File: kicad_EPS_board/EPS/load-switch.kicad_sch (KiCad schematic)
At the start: 18 parts, among them Q1 IPA045N10N3G, T1 BC846B, U1 INA186

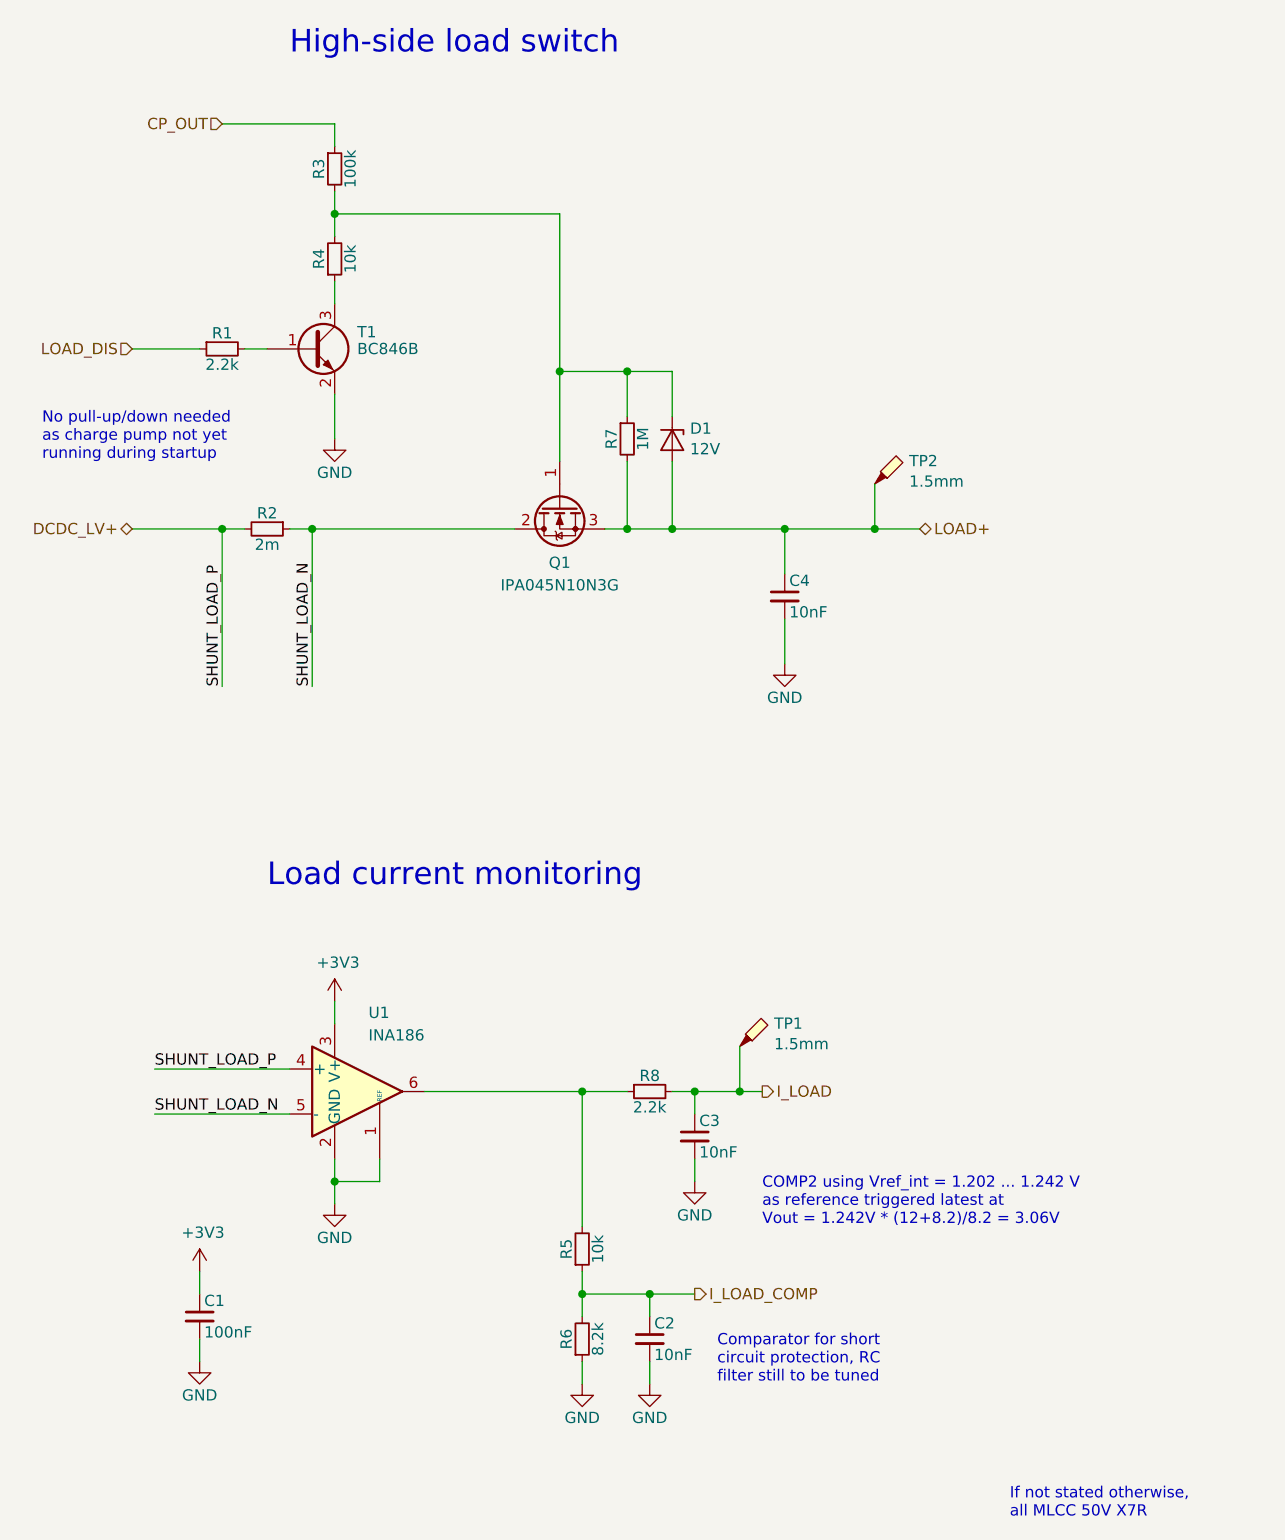
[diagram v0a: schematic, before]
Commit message: kicad EPS board V2 revision and already generated html doc files
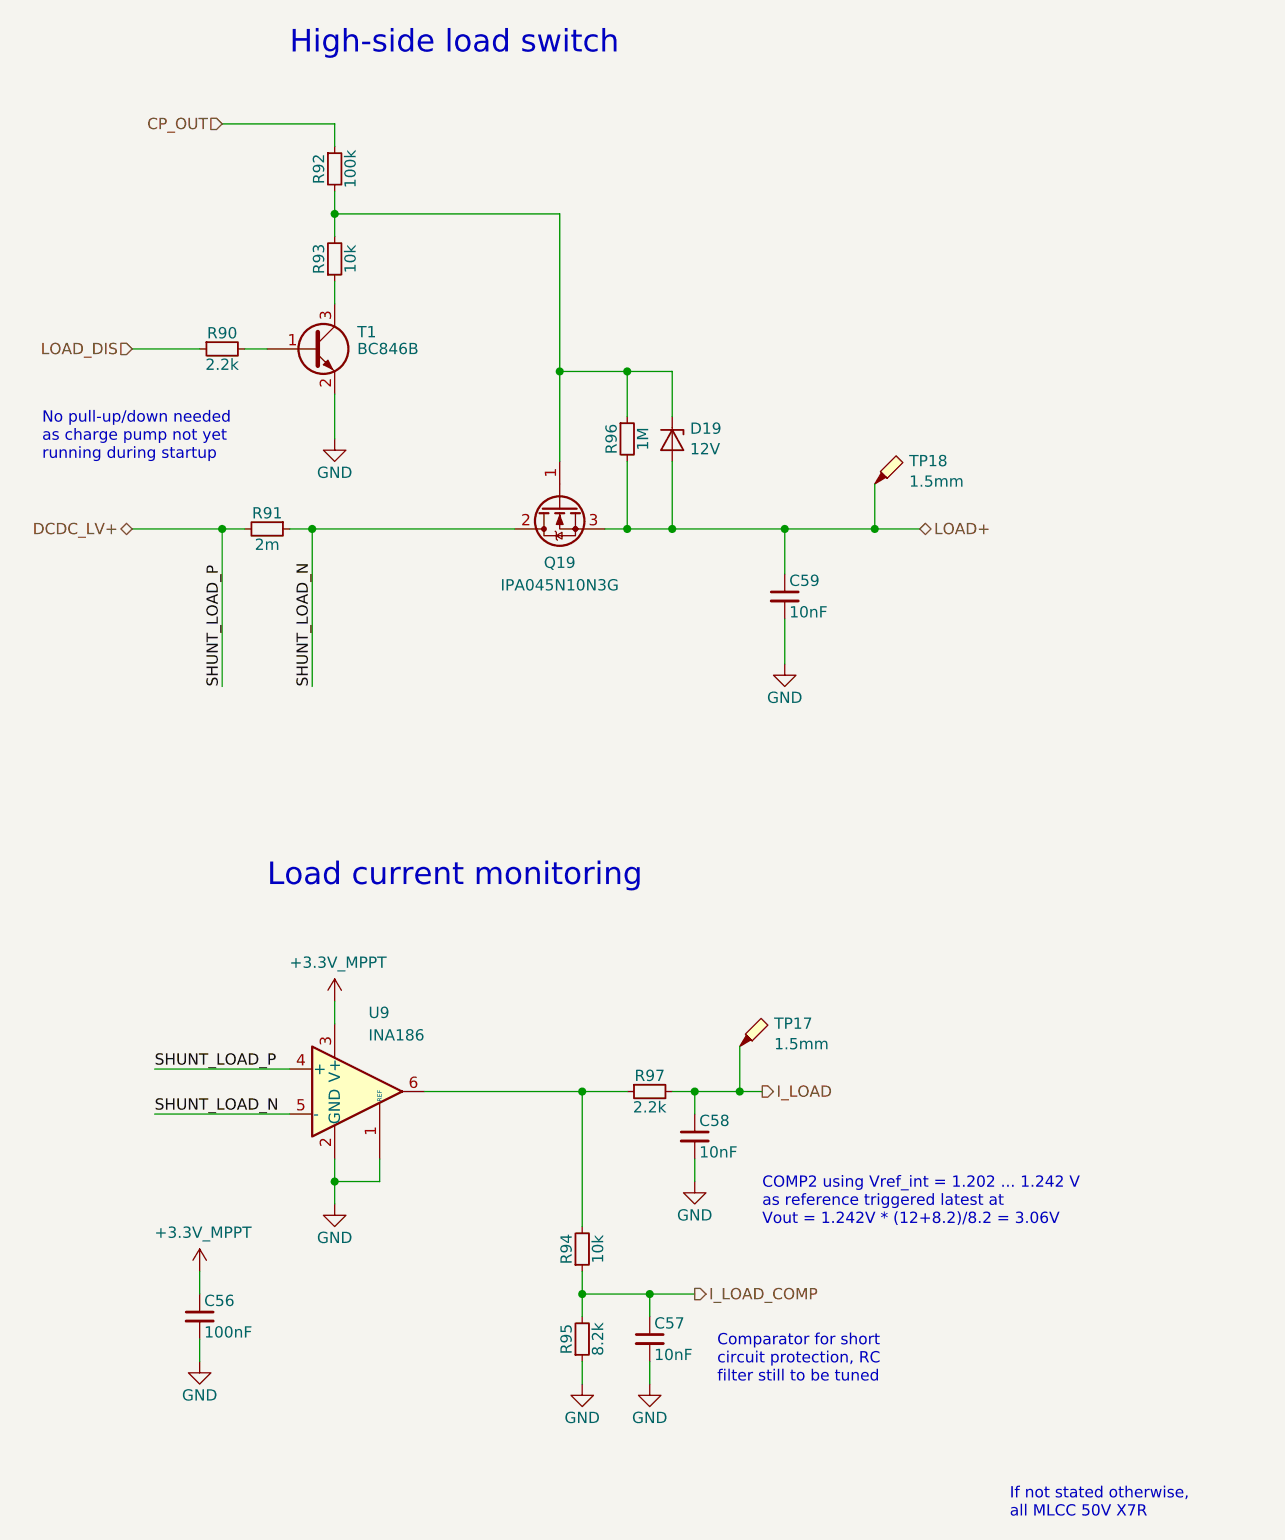
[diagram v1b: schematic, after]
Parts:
- renumbered C1 to C56, C2 to C57, C3 to C58, C4 to C59, D1 to D19, Q1 to Q19, R1 to R90, R2 to R91, R3 to R92, R4 to R93, R5 to R94, R6 to R95, R7 to R96, R8 to R97, TP1 to TP17, TP2 to TP18, U1 to U9
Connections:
- net +3V3 renamed +3.3V_MPPT
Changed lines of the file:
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@@
 (kicad_sch
-	(version 20231120)
+	(version 20250114)
 	(generator "eeschema")
-	(generator_version "8.0")
+	(generator_version "9.0")
 	(paper "A4")
+	(text "Load current monitoring"
+		(exclude_from_sim no)
+		(at 57.15 114.3 0)
+		(effects
+			(font
+				(size 2.54 2.54)
+			)
+			(justify left bottom)
+		)
+	)
+	(text "No pull-up/down needed\nas charge pump not yet \nrunning during startup"
+		(exclude_from_sim no)
+		(at 31.75 66.04 0)
+		(effects
+			(font
+				(size 1.27 1.27)
+			)
+			(justify left bottom)
+		)
+	)
+	(text "If not stated otherwise,\nall MLCC 50V X7R"
+		(exclude_from_sim no)
+		(at 140.97 185.42 0)
+		(effects
+			(font
+				(size 1.27 1.27)
+			)
+			(justify left bottom)
+		)
+	)
+	(text "Comparator for short \ncircuit protection, RC\nfilter still to be tuned"
+		(exclude_from_sim no)
+		(at 107.95 170.18 0)
+		(effects
+			(font
+				(size 1.27 1.27)
+			)
+			(justify left bottom)
+		)
+	)
+	(text "High-side load switch"
+		(exclude_from_sim no)
+		(at 59.69 20.32 0)
+		(effects
+			(font
+				(size 2.54 2.54)
+			)
+			(justify left bottom)
+		)
+	)
+	(text "COMP2 using Vref_int = 1.202 ... 1.242 V\nas reference triggered latest at\nVout = 1.242V * (12+8.2)/8.2 = 3.06V"
+		(exclude_from_sim no)
+		(at 113.03 152.4 0)
+		(effects
+			(font
+				(size 1.27 1.27)
+			)
+			(justify left bottom)
+		)
+	)
 	(junction
 		(at 62.23 73.66)
@@
 			(width 0)
 			(type default)
-		)
-	)
-	(text "Load current monitoring"
-		(exclude_from_sim no)
-		(at 57.15 114.3 0)
-		(effects
-			(font
-				(size 2.54 2.54)
-			)
-			(justify left bottom)
-		)
-	)
-	(text "No pull-up/down needed\nas charge pump not yet \nrunning during startup"
-		(exclude_from_sim no)
-		(at 31.75 66.04 0)
-		(effects
-			(font
-				(size 1.27 1.27)
-			)
-			(justify left bottom)
-		)
-	)
-	(text "If not stated otherwise,\nall MLCC 50V X7R"
-		(exclude_from_sim no)
-		(at 140.97 185.42 0)
-		(effects
-			(font
-				(size 1.27 1.27)
-			)
-			(justify left bottom)
-		)
-	)
-	(text "Comparator for short \ncircuit protection, RC\nfilter still to be tuned"
-		(exclude_from_sim no)
-		(at 107.95 170.18 0)
-		(effects
-			(font
-				(size 1.27 1.27)
-			)
-			(justify left bottom)
-		)
-	)
-	(text "High-side load switch"
-		(exclude_from_sim no)
-		(at 59.69 20.32 0)
-		(effects
-			(font
-				(size 2.54 2.54)
-			)
-			(justify left bottom)
-		)
-	)
-	(text "COMP2 using Vref_int = 1.202 ... 1.242 V\nas reference triggered latest at\nVout = 1.242V * (12+8.2)/8.2 = 3.06V"
-		(exclude_from_sim no)
-		(at 113.03 152.4 0)
-		(effects
-			(font
-				(size 1.27 1.27)
-			)
-			(justify left bottom)
 		)
 	)
@@
 		(on_board yes)
 		(dnp no)
-		(property "Reference" "C2"
+		(property "Reference" "C57"
 			(at 100.838 163.322 0)
 			(effects
@@
 		(on_board yes)
 		(dnp no)
-		(property "Reference" "TP1"
+		(property "Reference" "TP17"
 			(at 114.3762 129.4892 0)
 			(effects
@@
 		(on_board yes)
 		(dnp no)
-		(property "Reference" "TP2"
+		(property "Reference" "TP18"
 			(at 129.6162 65.9892 0)
 			(effects
@@
 		(on_board yes)
 		(dnp no)
-		(property "Reference" "#PWR03"
+		(property "Reference" "#PWR095"
 			(at 64.77 69.85 0)
 			(effects
@@
 		(on_board yes)
 		(dnp no)
-		(property "Reference" "R3"
+		(property "Reference" "R92"
 			(at 62.992 33.02 90)
 			(effects
@@
 		(on_board yes)
 		(dnp no)
-		(property "Reference" "R2"
+		(property "Reference" "R91"
 			(at 57.15 71.882 90)
 			(effects
@@
 		(on_board yes)
 		(dnp no)
-		(property "Reference" "C4"
+		(property "Reference" "C59"
 			(at 116.078 79.502 0)
 			(effects
@@
 		(on_board yes)
 		(dnp no)
-		(property "Reference" "D1"
+		(property "Reference" "D19"
 			(at 104.8766 62.3316 90)
 			(effects
@@
 		(on_board yes)
 		(dnp no)
-		(property "Reference" "R4"
+		(property "Reference" "R93"
 			(at 62.992 43.18 90)
 			(effects
@@
 		(on_board yes)
 		(dnp no)
-		(property "Reference" "#PWR02"
+		(property "Reference" "#PWR094"
 			(at 49.53 173.99 0)
 			(effects
@@
 		(on_board yes)
 		(dnp no)
-		(property "Reference" "R6"
+		(property "Reference" "R95"
 			(at 90.932 165.1 90)
 			(effects
@@
 		(on_board yes)
 		(dnp no)
-		(property "Reference" "#PWR01"
+		(property "Reference" "#PWR093"
 			(at 49.53 161.29 0)
 			(effects
@@
 			)
 		)
-		(property "Value" "+3V3"
+		(property "Value" "+3.3V_MPPT"
 			(at 49.911 153.0858 0)
 			(effects
@@
 		(on_board yes)
 		(dnp no)
-		(property "Reference" "Q1"
+		(property "Reference" "Q19"
 			(at 90.17 77.47 90)
 			(effects
@@
 		(on_board yes)
 		(dnp no)
-		(property "Reference" "#PWR04"
+		(property "Reference" "#PWR096"
 			(at 64.77 130.81 0)
 			(effects
@@
 			)
 		)
-		(property "Value" "+3V3"
+		(property "Value" "+3.3V_MPPT"
 			(at 65.151 122.6058 0)
 			(effects
@@
 		(on_board yes)
 		(dnp no)
-		(property "Reference" "R8"
+		(property "Reference" "R97"
 			(at 100.33 135.382 90)
 			(effects
@@
 		(on_board yes)
 		(dnp no)
-		(property "Reference" "#PWR05"
+		(property "Reference" "#PWR097"
 			(at 64.77 156.21 0)
 			(effects
@@
 		(on_board yes)
 		(dnp no)
-		(property "Reference" "U1"
+		(property "Reference" "U9"
 			(at 68.58 128.27 0)
 			(effects
@@
 		(on_board yes)
 		(dnp no)
-		(property "Reference" "R5"
+		(property "Reference" "R94"
 			(at 90.932 154.94 90)
 			(effects
@@
 		(on_board yes)
 		(dnp no)
-		(property "Reference" "#PWR08"
+		(property "Reference" "#PWR0100"
 			(at 105.41 153.67 0)
 			(effects
@@
 		(on_board yes)
 		(dnp no)
-		(property "Reference" "R7"
+		(property "Reference" "R96"
 			(at 96.012 63.5 90)
 			(effects
@@
 		(on_board yes)
 		(dnp no)
-		(property "Reference" "#PWR09"
+		(property "Reference" "#PWR0101"
 			(at 115.57 95.25 0)
 			(effects
@@
 		(on_board yes)
 		(dnp no)
-		(property "Reference" "C1"
+		(property "Reference" "C56"
 			(at 50.038 160.782 0)
 			(effects
@@
 		(on_board yes)
 		(dnp no)
-		(property "Reference" "#PWR07"
+		(property "Reference" "#PWR099"
 			(at 100.33 176.53 0)
 			(effects
@@
 		(on_board yes)
 		(dnp no)
-		(property "Reference" "C3"
+		(property "Reference" "C58"
 			(at 105.918 140.462 0)
 			(effects
@@
 		(on_board yes)
 		(dnp no)
-		(property "Reference" "#PWR06"
+		(property "Reference" "#PWR098"
 			(at 92.71 176.53 0)
 			(effects
@@
 		(on_board yes)
 		(dnp no)
-		(property "Reference" "R1"
+		(property "Reference" "R90"
 			(at 52.07 51.562 90)
 			(effects
